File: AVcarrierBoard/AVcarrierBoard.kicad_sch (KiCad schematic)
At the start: 18 parts, among them J1 Mech_Switch, J2 Mech_Switch, J3 MainRecov, J4 DrogRecov, J5 Staging, J6 Mech_Switch, U2 WiFi Switch, U3 EggtimerQuantum, U4 EggfinderMini/FeatherGPS, U5 Blue_Raven

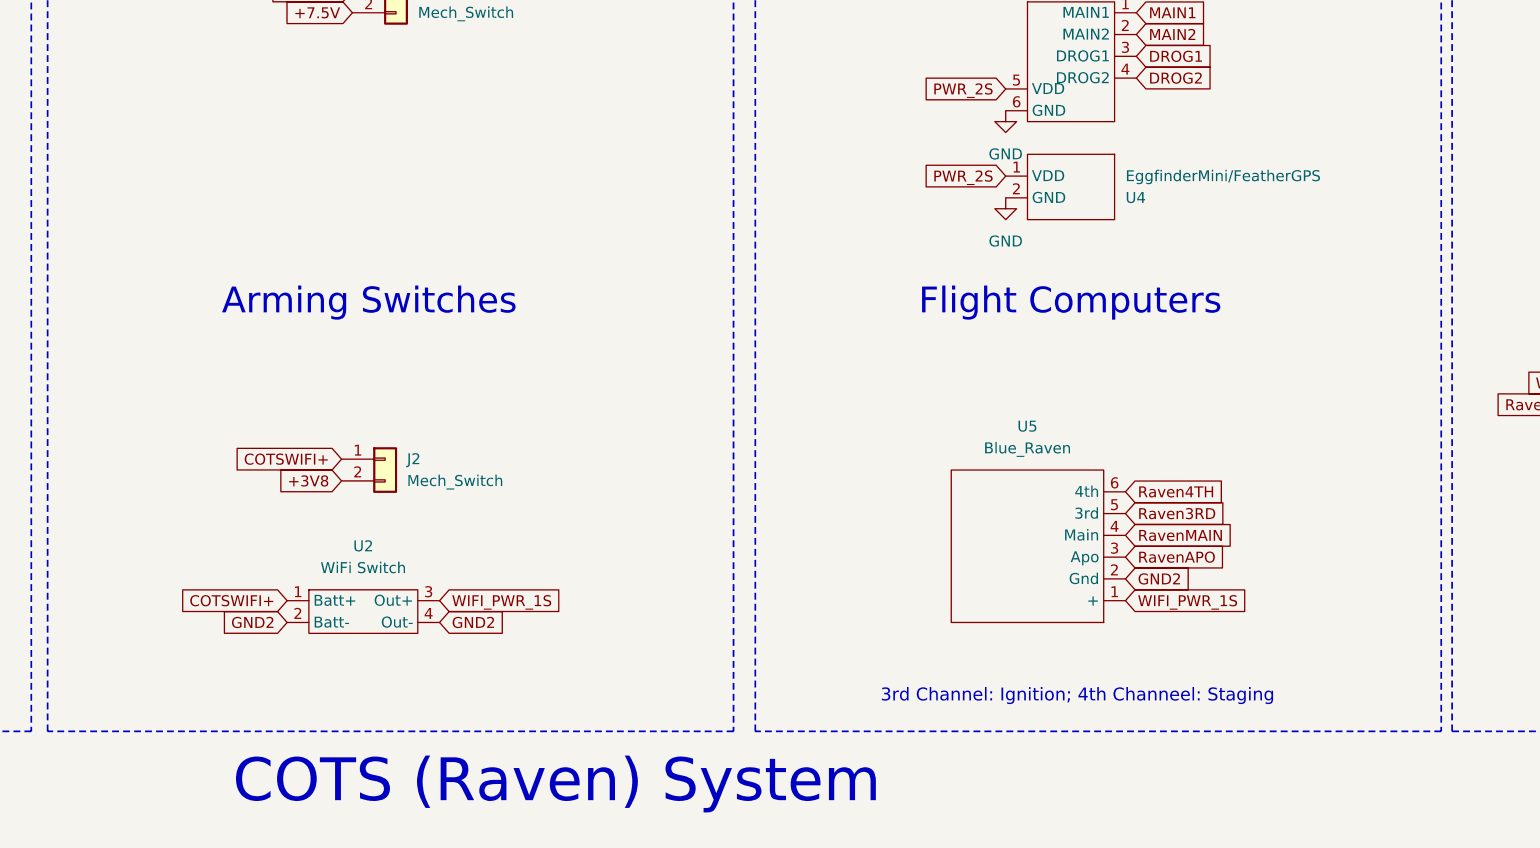
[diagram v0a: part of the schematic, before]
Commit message: changes to blue raven orientation, radio power, wifi gnd, etc.
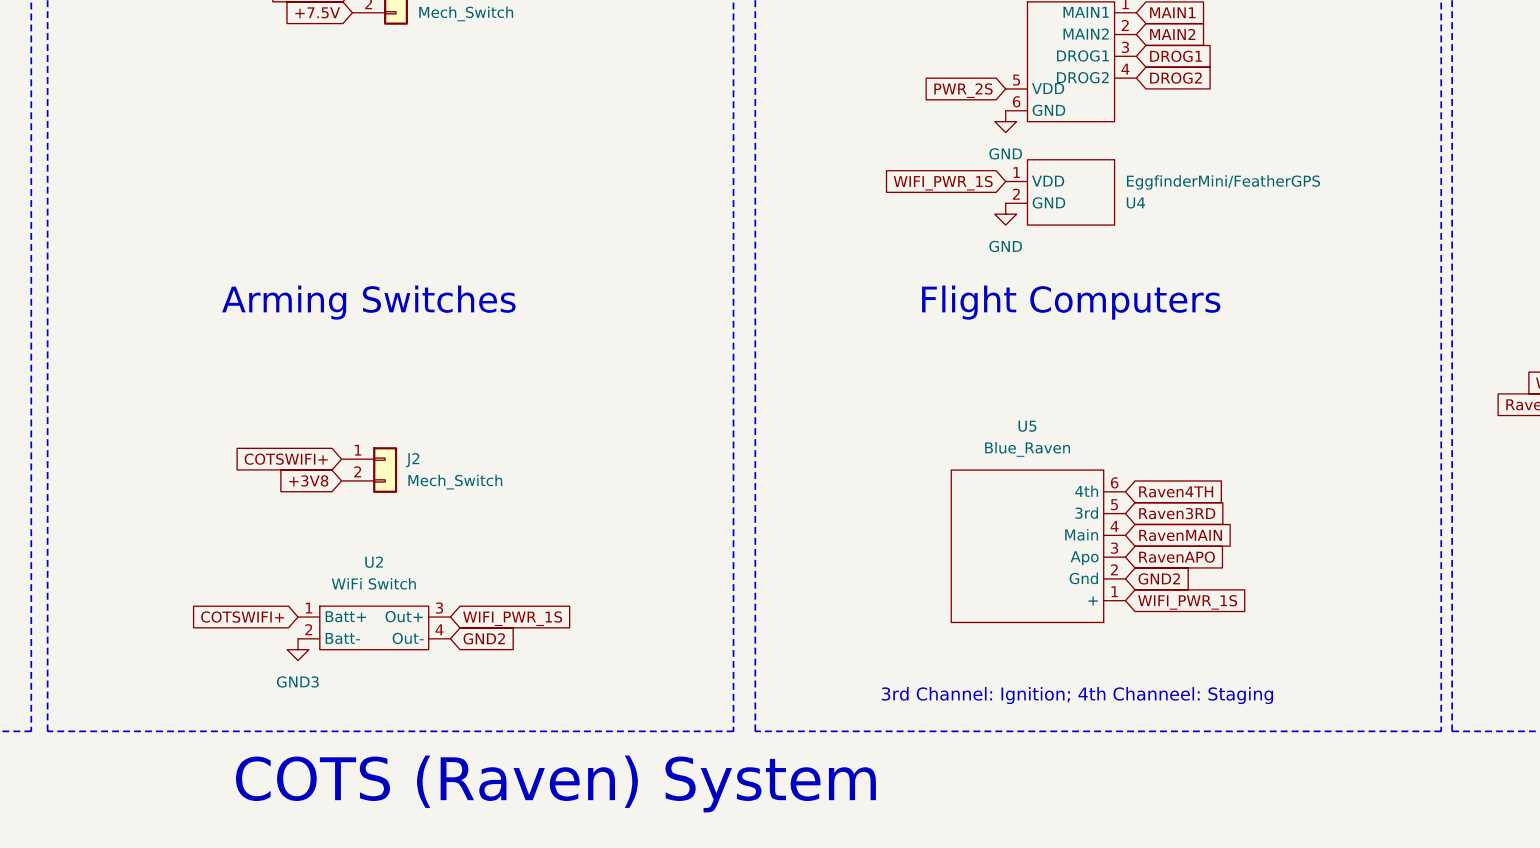
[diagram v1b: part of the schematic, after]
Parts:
- J1, J2: footprint 2.97mmConnector:PinHeader_1x02_P2.97mm_Vertical -> COTS_Boards:CON_436500227_MOL
- J6: footprint Connector_PinHeader_2.54mm:PinHeader_1x02_P2.54mm_Vertical -> COTS_Boards:CON_436500227_MOL
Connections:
- net GND2: no longer U2.2 (Batt-)
- net PWR_2S: no longer U4.1 (VDD)
- net WIFI_PWR_1S: now also U4.1 (VDD)
- new net GND3: U2.2 (Batt-)
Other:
- moved on the sheet: U2, U4
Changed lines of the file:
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@@
-    )
-  )
-  (global_label "GND2" (shape input) (at 86.36 117.475 180) (fields_autoplaced)
-    (effects (font (size 1.27 1.27)) (justify right))
-    (property "Intersheetrefs" "${INTERSHEET_REFS}" (at 78.2948 117.475 0)
-      (effects (font (size 1.27 1.27)) (justify right) hide)
     )
   )
@@
     )
   )
-  (global_label "COTSWIFI+" (shape input) (at 86.36 114.935 180) (fields_autoplaced)
-    (effects (font (size 1.27 1.27)) (justify right))
-    (property "Intersheetrefs" "${INTERSHEET_REFS}" (at 73.2752 114.935 0)
+  (global_label "COTSWIFI+" (shape input) (at 87.63 116.84 180) (fields_autoplaced)
+    (effects (font (size 1.27 1.27)) (justify right))
+    (property "Intersheetrefs" "${INTERSHEET_REFS}" (at 74.5452 116.84 0)
       (effects (font (size 1.27 1.27)) (justify right) hide)
     )
@@
     )
   )
-  (global_label "PWR_2S" (shape input) (at 170.18 65.405 180) (fields_autoplaced)
-    (effects (font (size 1.27 1.27)) (justify right))
-    (property "Intersheetrefs" "${INTERSHEET_REFS}" (at 159.8168 65.405 0)
-      (effects (font (size 1.27 1.27)) (justify right) hide)
-    )
-  )
   (global_label "RavenMotIgnition" (shape input) (at 245.11 92.075 180) (fields_autoplaced)
     (effects (font (size 1.27 1.27)) (justify right))
@@
     )
   )
-  (global_label "WIFI_PWR_1S" (shape input) (at 104.14 114.935 0) (fields_autoplaced)
-    (effects (font (size 1.27 1.27)) (justify left))
-    (property "Intersheetrefs" "${INTERSHEET_REFS}" (at 119.2204 114.935 0)
+  (global_label "WIFI_PWR_1S" (shape input) (at 105.41 116.84 0) (fields_autoplaced)
+    (effects (font (size 1.27 1.27)) (justify left))
+    (property "Intersheetrefs" "${INTERSHEET_REFS}" (at 120.4904 116.84 0)
       (effects (font (size 1.27 1.27)) (justify left) hide)
     )
@@
     )
   )
-  (global_label "GND2" (shape input) (at 104.14 117.475 0) (fields_autoplaced)
-    (effects (font (size 1.27 1.27)) (justify left))
-    (property "Intersheetrefs" "${INTERSHEET_REFS}" (at 112.2052 117.475 0)
+  (global_label "WIFI_PWR_1S" (shape input) (at 170.18 66.04 180) (fields_autoplaced)
+    (effects (font (size 1.27 1.27)) (justify right))
+    (property "Intersheetrefs" "${INTERSHEET_REFS}" (at 155.0996 66.04 0)
+      (effects (font (size 1.27 1.27)) (justify right) hide)
+    )
+  )
+  (global_label "GND2" (shape input) (at 105.41 119.38 0) (fields_autoplaced)
+    (effects (font (size 1.27 1.27)) (justify left))
+    (property "Intersheetrefs" "${INTERSHEET_REFS}" (at 113.4752 119.38 0)
       (effects (font (size 1.27 1.27)) (justify left) hide)
     )
@@
       (effects (font (size 1.27 1.27)) (justify left))
     )
-    (property "Footprint" "Connector_PinHeader_2.54mm:PinHeader_1x02_P2.54mm_Vertical" (at 144.78 161.29 0)
+    (property "Footprint" "COTS_Boards:CON_436500227_MOL" (at 144.78 161.29 0)
       (effects (font (size 1.27 1.27)) hide)
     )
@@
     )
   )
-  (symbol (lib_id "power:GND") (at 170.18 67.945 0) (unit 1)
-    (in_bom yes) (on_board yes) (dnp no) (fields_autoplaced)
-    (property "Reference" "#PWR05" (at 170.18 74.295 0)
-      (effects (font (size 1.27 1.27)) hide)
-    )
-    (property "Value" "GND" (at 170.18 73.025 0)
-      (effects (font (size 1.27 1.27)))
-    )
-    (property "Footprint" "" (at 170.18 67.945 0)
-      (effects (font (size 1.27 1.27)) hide)
-    )
-    (property "Datasheet" "" (at 170.18 67.945 0)
+  (symbol (lib_id "power:GND") (at 170.18 68.58 0) (unit 1)
+    (in_bom yes) (on_board yes) (dnp no) (fields_autoplaced)
+    (property "Reference" "#PWR05" (at 170.18 74.93 0)
+      (effects (font (size 1.27 1.27)) hide)
+    )
+    (property "Value" "GND" (at 170.18 73.66 0)
+      (effects (font (size 1.27 1.27)))
+    )
+    (property "Footprint" "" (at 170.18 68.58 0)
+      (effects (font (size 1.27 1.27)) hide)
+    )
+    (property "Datasheet" "" (at 170.18 68.58 0)
       (effects (font (size 1.27 1.27)) hide)
     )
@@
       (effects (font (size 1.27 1.27)) (justify left))
     )
-    (property "Footprint" "2.97mmConnector:PinHeader_1x02_P2.97mm_Vertical" (at 99.06 43.815 0)
+    (property "Footprint" "COTS_Boards:CON_436500227_MOL" (at 99.06 43.815 0)
       (effects (font (size 1.27 1.27)) hide)
     )
@@
       (effects (font (size 1.27 1.27)) (justify left))
     )
-    (property "Footprint" "2.97mmConnector:PinHeader_1x02_P2.97mm_Vertical" (at 97.79 98.425 0)
+    (property "Footprint" "COTS_Boards:CON_436500227_MOL" (at 97.79 98.425 0)
       (effects (font (size 1.27 1.27)) hide)
     )
@@
     )
   )
-  (symbol (lib_id "COTS_boards:EggfinderMini") (at 182.88 62.865 0) (mirror y) (unit 1)
+  (symbol (lib_id "power:GND3") (at 87.63 119.38 0) (unit 1)
+    (in_bom yes) (on_board yes) (dnp no) (fields_autoplaced)
+    (property "Reference" "#PWR02" (at 87.63 125.73 0)
+      (effects (font (size 1.27 1.27)) hide)
+    )
+    (property "Value" "GND3" (at 87.63 124.46 0)
+      (effects (font (size 1.27 1.27)))
+    )
+    (property "Footprint" "" (at 87.63 119.38 0)
+      (effects (font (size 1.27 1.27)) hide)
+    )
+    (property "Datasheet" "" (at 87.63 119.38 0)
+      (effects (font (size 1.27 1.27)) hide)
+    )
+    (pin "1")
+    (instances
+      (project "AVcarrierBoard"
+        (path "/7d4c9aa4-eccf-4732-8f5d-af2c3b6d9138"
+          (reference "#PWR02") (unit 1)
+        )
+      )
+    )
+  )
+  (symbol (lib_id "COTS_boards:EggfinderMini") (at 182.88 63.5 0) (mirror y) (unit 1)
     (in_bom yes) (on_board yes) (dnp no)
-    (property "Reference" "U4" (at 184.15 67.945 0)
+    (property "Reference" "U4" (at 184.15 68.58 0)
       (effects (font (size 1.27 1.27)) (justify right))
     )
-    (property "Value" "EggfinderMini/FeatherGPS" (at 184.15 65.405 0)
+    (property "Value" "EggfinderMini/FeatherGPS" (at 184.15 66.04 0)
       (effects (font (size 1.27 1.27)) (justify right))
     )
-    (property "Footprint" "COTS_Boards:Featherweight_GPS" (at 176.53 71.755 0)
-      (effects (font (size 1.27 1.27)) hide)
-    )
-    (property "Datasheet" "" (at 182.88 62.865 0)
+    (property "Footprint" "COTS_Boards:Featherweight_GPS" (at 176.53 72.39 0)
+      (effects (font (size 1.27 1.27)) hide)
+    )
+    (property "Datasheet" "" (at 182.88 63.5 0)
       (effects (font (size 1.27 1.27)) hide)
     )
@@
     )
   )
-  (symbol (lib_id "COTS_boards:Eggtimer_WiFi_switch") (at 95.25 114.935 0) (unit 1)
-    (in_bom yes) (on_board yes) (dnp no) (fields_autoplaced)
-    (property "Reference" "U2" (at 95.25 108.585 0)
-      (effects (font (size 1.27 1.27)))
-    )
-    (property "Value" "WiFi Switch" (at 95.25 111.125 0)
-      (effects (font (size 1.27 1.27)))
-    )
-    (property "Footprint" "COTS_Boards:Eggtime_WiFi_switch" (at 95.25 114.935 0)
-      (effects (font (size 1.27 1.27)) hide)
-    )
-    (property "Datasheet" "https://eggtimerrocketry.com/eggtimer-mini-switch-support/" (at 95.25 116.205 0)
-      (effects (font (size 1.27 1.27)) hide)
-    )
+  (symbol (lib_id "COTS_boards:Eggtimer_WiFi_switch") (at 96.52 116.84 0) (unit 1)
+    (in_bom yes) (on_board yes) (dnp no) (fields_autoplaced)
+    (property "Reference" "U2" (at 96.52 110.49 0)
+      (effects (font (size 1.27 1.27)))
+    )
+    (property "Value" "WiFi Switch" (at 96.52 113.03 0)
+      (effects (font (size 1.27 1.27)))
+    )
+    (property "Footprint" "COTS_Boards:Eggtime_WiFi_switch" (at 96.52 116.84 0)
+      (effects (font (size 1.27 1.27)) hide)
+    )
+    (property "Datasheet" "https://eggtimerrocketry.com/eggtimer-mini-switch-support/" (at 96.52 118.11 0)
+      (effects (font (size 1.27 1.27)) hide)
+    )
